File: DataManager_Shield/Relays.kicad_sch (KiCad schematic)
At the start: 57 parts, among them J1 CAR_IN, J3 CAR_OUT, J4 Mode_Selector, K1 IM03, K2 IM03, Q10 AO3400A, Q9 AO3400A, U1 TLP291-4, U2 MCP4725xxx-xCH, U3 TLP291-4, U4 PCA9306

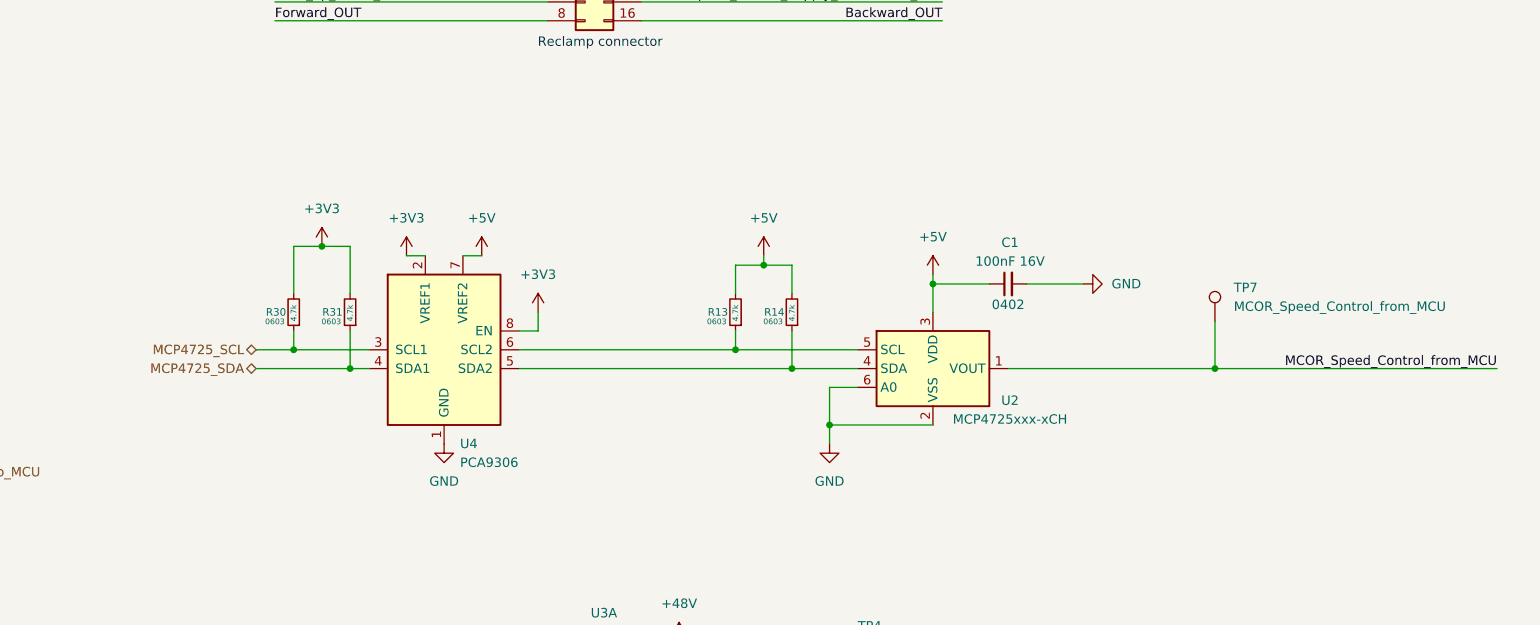
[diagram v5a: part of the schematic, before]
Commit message: Isolate GND for Datamanager Shield
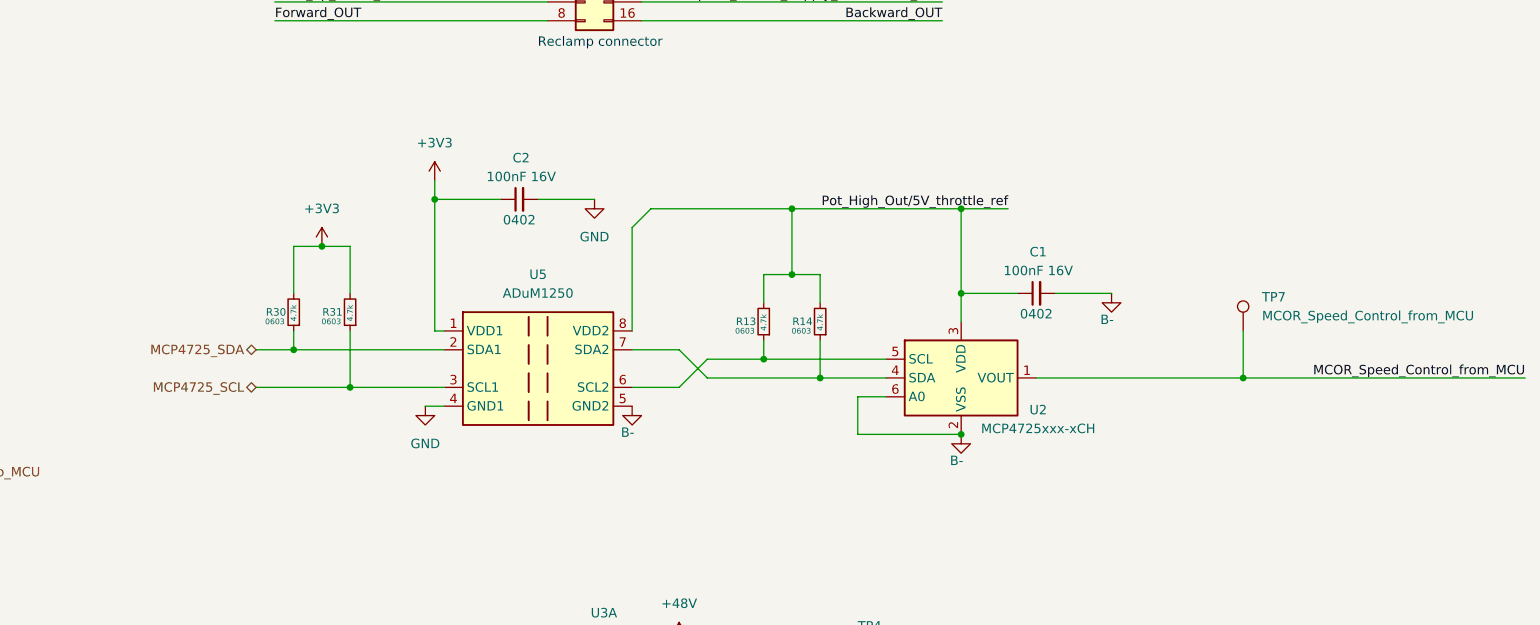
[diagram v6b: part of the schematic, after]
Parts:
- removed U4: PCA9306, Package_SO:VSSOP-8_2.3x2mm_P0.5mm, symbol Interface:PCA9306
- added C2: 100nF 16V, Capacitor_SMD:C_0402_1005Metric, symbol Device:C_Small
- added U5: ADuM1250, Package_SO:SOIC-8_3.9x4.9mm_P1.27mm, symbol Isolator:ADuM1250
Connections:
- net +3V3: now also C2.1, U5.1 (VDD1)
- net +5V: no longer C1.1, R13.2, R14.2, U2.3 (VDD)
- net B-: now also C1.2, U2.2 (VSS), U2.6 (A0), U5.5 (GND2)
- net GND: now also C2.2, U5.4 (GND1); no longer C1.2, U2.2 (VSS), U2.6 (A0)
- net MCP4725_SCL: now also R31.1, U5.3 (SCL1); no longer R30.1
- net MCP4725_SDA: now also R30.1, U5.2 (SDA1); no longer R31.1
- net Pot_High_Out/5V_throttle_ref: now also C1.1, R13.2, R14.2, U2.3 (VDD), U5.8 (VDD2)
- net at R14.1, U2.4 (SDA): now also U5.7 (SDA2)
- net at R13.1, U2.5 (SCL): now also U5.6 (SCL2)
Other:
- moved on the sheet: C1, R13, R14, TP7, U2
